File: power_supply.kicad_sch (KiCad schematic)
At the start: 7 parts

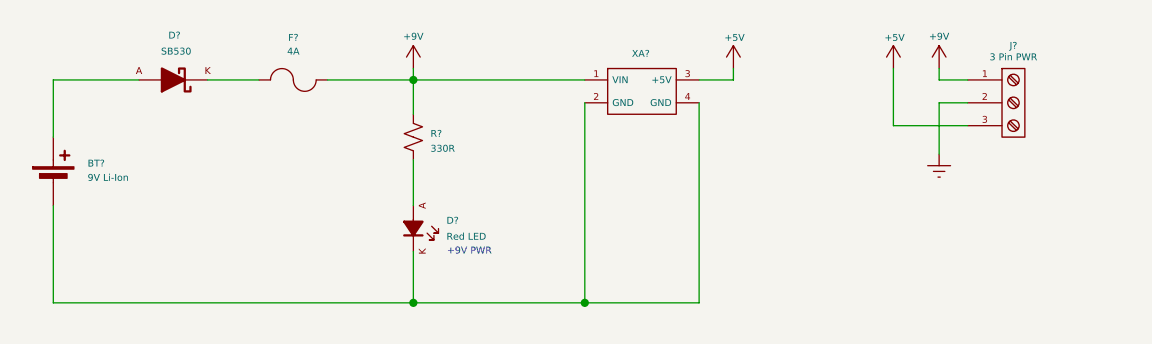
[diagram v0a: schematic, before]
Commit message: Finished All footprints - PCB placement done momemtarily - plus wiring buck convertor done
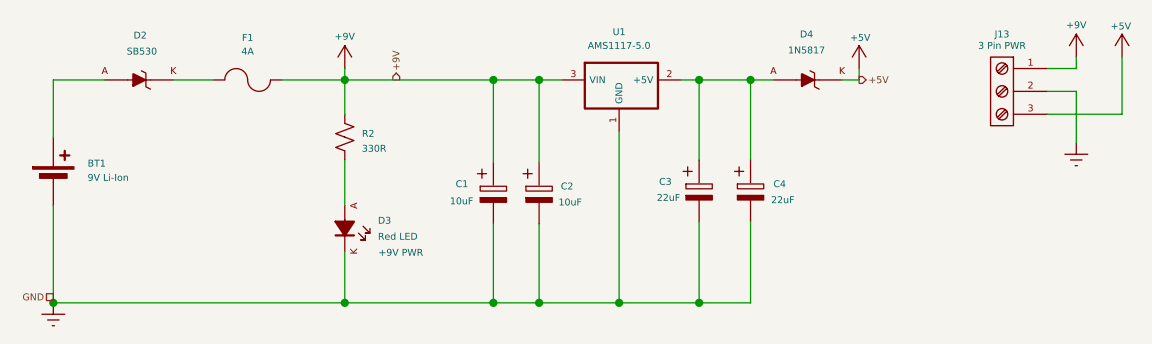
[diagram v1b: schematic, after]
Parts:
- removed XA?: ~, symbol Custom Parts:Buck_Convertor_Module
- added C1, C2: 10uF, Capacitor_Tantalum_SMD:CP_EIA-3216-18_Kemet-A, symbol PCM_Capacitor_AKL:CP_Generic
- added C3, C4: 22uF, Capacitor_Tantalum_SMD:CP_EIA-3216-18_Kemet-A, symbol PCM_Capacitor_AKL:CP_Generic
- added D4: 1N5817, PCM_Diode_THT_AKL:D_DO-41_SOD81_P10.16mm_Horizontal, symbol PCM_Diode_Schottky_AKL:1N5817
- added U1: AMS1117-5.0, Package_TO_SOT_SMD:SOT-223-3_TabPin2, symbol Regulator_Linear:AMS1117-5.0
- D2: renamed from D?; footprint Diode_THT:D_DO-41_SOD81_P10.16mm_Horizontal -> Diode_THT:D_DO-201AD_P15.24mm_Horizontal
- J13: renamed from J?; footprint 4ms_Connector:Pins_1x03_2.54mm_TH_AudioInsRGndL -> Library:KEFA_KF2EDGR_3.81_3P; now left out of the parts list
- R2: renamed from R?; footprint PCM_Resistor_THT_AKL:R_Axial_DIN0411_L9.9mm_D3.6mm_P12.70mm_Horizontal -> PCM_Resistor_THT_AKL:R_Axial_DIN0309_L9.0mm_D3.2mm_P12.70mm_Horizontal
- gave numbers to parts that had none: 3
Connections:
- net +5V: now also D4.1 (K)
- net +9V: now also C1.1, C2.1, U1.3 (VIN)
- net GNDREF: now also BT1.2 (-), D3.1 (K), C1.2, C2.2, C3.2, C4.2, U1.1 (GND)
- new net: C3.1, C4.1, D4.2 (A), U1.2 (+5V)
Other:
- moved on the sheet: D2, D3, F1, J13, R2
